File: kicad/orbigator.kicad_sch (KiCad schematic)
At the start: 0 parts

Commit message: KiCad schematic WiP
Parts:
- added BT1: CR2032, symbol Device:Battery_Cell
- added DISP1: OLED_Encoder, symbol orbigator:OLED_Encoder
- added M1: DYNAMIXEL_1, symbol Connector_Generic:Conn_01x03
- added M2: DYNAMIXEL_2, symbol Connector_Generic:Conn_01x03
- added R1, R2, R3: 10k, symbol PCM_Elektuur:R
- added RTC1: DS3232, symbol orbigator:Adafruit_DS3231_Breakout
- added U1: Pico_2, Module_RaspberryPi_Pico:RaspberryPi_Pico_Original_SMD_HandSolder, symbol MCU_Module_RaspberryPi_Pico:RaspberryPi_Pico_DebugPins
- added U2: 74LS126, symbol 74xx:74LS126
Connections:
- new net 3V3: DISP1.9 (VCC), R2.1 (+), R3.1 (+), RTC1.1 (Vin), U1.36 (3V3), U2.14 (VCC)
- new net 3V_BAT: BT1.1 (+), RTC1.5 (BAT)
- new net 5V0: M1.2 (Pin_2), M2.2 (Pin_2), R1.1 (+), U1.40 (VBUS)
- new net 5V_SYS: U1.39 (VSYS)
- new net BAK_BTN: DISP1.7 (BAK_BTN), U1.12 (GPIO9)
- new net CNF_BTN: DISP1.1 (CNF_BTN), U1.14 (GPIO10)
- new net DIR: U1.4 (GPIO2), U2.1
- new net ENC_A: DISP1.5 (ENC_A), U1.9 (GPIO6)
- new net ENC_B: DISP1.6 (ENC_B), U1.10 (GPIO7)
- new net ENC_SW: DISP1.4 (ENC_SW), U1.11 (GPIO8)
- new net GND: BT1.2 (-), DISP1.8 (GND), M1.1 (Pin_1), M2.1 (Pin_1), RTC1.2 (GND), U1.13 (GND), U1.18 (GND), U1.23 (GND), U1.28 (GND), U1.3 (GND), U1.38 (GND), U1.8 (GND), U1.D2 (GND), U2.10, U2.12, U2.13, U2.4, U2.5, U2.7 (GND), U2.9
- new net MOT_DAT: M1.3 (Pin_3), M2.3 (Pin_3), R1.2 (-), U1.2 (GPIO1), U2.3
- new net SCL: DISP1.3 (SCL), R2.2 (-), RTC1.3 (SCL), U1.7 (GPIO5)
- new net SDA: DISP1.2 (SDA), R3.2 (-), RTC1.4 (SDA), U1.6 (GPIO4)
- new net UART_TX: U1.1 (GPIO0), U2.2
- no-connect marks 0 -> 3
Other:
- company: WyoLum -> (none)
- title: Orbigator Controller -> (none)

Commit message: schematic done
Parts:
- added J1: Conn_01x01, symbol orbigator:Conn_01x01
- added J10: Conn_01x01, symbol orbigator:Conn_01x01_16
- added J11: Conn_01x01, symbol orbigator:Conn_01x01_15
- added J12: Conn_01x01, symbol orbigator:Conn_01x01_14
- added J13: Conn_01x01, symbol orbigator:Conn_01x01_13
- added J14: Conn_01x01, symbol orbigator:Conn_01x01_12
- added J15: Conn_01x01, symbol orbigator:Conn_01x01_11
- added J16: Conn_01x01, symbol orbigator:Conn_01x01_10
- added J17: Conn_01x01, symbol orbigator:Conn_01x01_9
- added J18: Conn_01x01, symbol orbigator:Conn_01x01_8
- added J19: Conn_01x01, symbol orbigator:Conn_01x01_7
- added J2: Conn_01x01, symbol orbigator:Conn_01x01_24
- added J20: Conn_01x01, symbol orbigator:Conn_01x01_6
- added J21: Conn_01x01, symbol orbigator:Conn_01x01_5
- added J22: Conn_01x01, symbol orbigator:Conn_01x01_4
- added J23: Conn_01x01, symbol orbigator:Conn_01x01_3
- added J24: Conn_01x01, symbol orbigator:Conn_01x01_2
- added J25, J26, J27, J28, J29: Conn_01x01, symbol orbigator:Conn_01x01_1
- added J3: Conn_01x01, symbol orbigator:Conn_01x01_23
- added J4: Conn_01x01, symbol orbigator:Conn_01x01_22
- added J5: Conn_01x01, symbol orbigator:Conn_01x01_21
- added J6: Conn_01x01, symbol orbigator:Conn_01x01_20
- added J7: Conn_01x01, symbol orbigator:Conn_01x01_19
- added J8: Conn_01x01, symbol orbigator:Conn_01x01_18
- added J9: Conn_01x01, symbol orbigator:Conn_01x01_17
- BT1: symbol Device:Battery_Cell -> orbigator:Battery_Cell
- M1, M2: symbol Connector_Generic:Conn_01x03 -> orbigator:Conn_01x03
- R1, R2, R3: symbol PCM_Elektuur:R -> orbigator:R
- U1: symbol MCU_Module_RaspberryPi_Pico:RaspberryPi_Pico_DebugPins -> orbigator:RaspberryPi_Pico_DebugPins
- U2: symbol 74xx:74LS126 -> orbigator:74LS126
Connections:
- net 3V3: now also R1.1 (+), J23.1 (Pin_1)
- net 5V0: now also J25.1 (Pin_1); no longer R1.1 (+)
- net 5V_SYS: now also J24.1 (Pin_1)
- net GND: now also J26.1 (Pin_1)
- net at U1.15 (GPIO11): now also J19.1 (Pin_1)
- net at U1.16 (GPIO12): now also J18.1 (Pin_1)
- net at U1.17 (GPIO13): now also J17.1 (Pin_1)
- net at U1.19 (GPIO14): now also J16.1 (Pin_1)
- net at U1.20 (GPIO15): now also J15.1 (Pin_1)
- net at U1.21 (GPIO16): now also J1.1 (Pin_1)
- net at U1.22 (GPIO17): now also J2.1 (Pin_1)
- net at U1.24 (GPIO18): now also J3.1 (Pin_1)
- net at U1.25 (GPIO19): now also J4.1 (Pin_1)
- net at U1.26 (GPIO20): now also J5.1 (Pin_1)
- net at U1.27 (GPIO21): now also J6.1 (Pin_1)
- net at U1.29 (GPIO22): now also J7.1 (Pin_1)
- net at U1.30 (RUN): now also J14.1 (Pin_1)
- net at U1.31 (GPIO26_ADC0): now also J9.1 (Pin_1)
- net at U1.32 (GPIO27_ADC1): now also J10.1 (Pin_1)
- net at U1.33 (AGND): now also J12.1 (Pin_1)
- net at U1.34 (GPIO28_ADC2): now also J11.1 (Pin_1)
- net at U1.35 (ADC_VREF): now also J8.1 (Pin_1)
- net at U1.37 (3V3_EN): now also J13.1 (Pin_1)
- net at U1.5 (GPIO3): now also J20.1 (Pin_1)
- net at U1.D1 (SWCLK): now also J22.1 (Pin_1)
- net at U1.D3 (SWDIO): now also J21.1 (Pin_1)
- net at RTC1.6 (32k): now also J27.1 (Pin_1)
- net at RTC1.7 (SQW): now also J28.1 (Pin_1)
- net at RTC1.8 (RST): now also J29.1 (Pin_1)
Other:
- company: (none) -> Wyolum
- title: (none) -> Orbigator PCB

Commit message: PCB layout WiP
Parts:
- removed BT1: CR2032, symbol orbigator:Battery_Cell
- removed J27, J28, J29: Conn_01x01, symbol orbigator:Conn_01x01_1
- removed RTC1: DS3232, symbol orbigator:Adafruit_DS3231_Breakout
- added H1, H2, H3, H4: MountingHole, orbigator:MountingHole_3.2mm_M3, symbol Mechanical:MountingHole
- added RTC1: DS3232, orbigator:DS3232_RTC, symbol Connector_Generic:Conn_01x07
- DISP1: footprint (none) -> orbigator:PinSocket_1x09_P2.54mm_Vertical
- J1, J10, J11, J12, J13, J14, J15, J16, J17, J18, J19, J2, J20, J21, J22, J23, J24, J25, J26, J3, J4, J5, J6, J7, J8, J9: footprint (none) -> orbigator:PinHeader_1x01_P2.54mm_Vertical
- M1, M2: footprint (none) -> orbigator:JST_GH_BM03B-GHS-TBT_1x03-1MP_P1.25mm_Vertical
- R1, R2, R3: footprint (none) -> orbigator:R_Axial_DIN0207_L6.3mm_D2.5mm_P7.62mm_Horizontal
- U1: footprint Module_RaspberryPi_Pico:RaspberryPi_Pico_Original_SMD_HandSolder -> orbigator:RaspberryPi_Pico_SMD_HandSolder
- U2: footprint (none) -> orbigator:DIP-14_W7.62mm
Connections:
- net 3V3: now also RTC1.1 (Pin_1)
- net GND: now also RTC1.2 (Pin_2)
- net SCL: now also RTC1.3 (Pin_3)
- net SDA: now also RTC1.4 (Pin_4)
- new net 32k: RTC1.7 (Pin_7)
- new net INT: RTC1.5 (Pin_5)
- new net RST: RTC1.6 (Pin_6)
- no-connect marks 3 -> 6

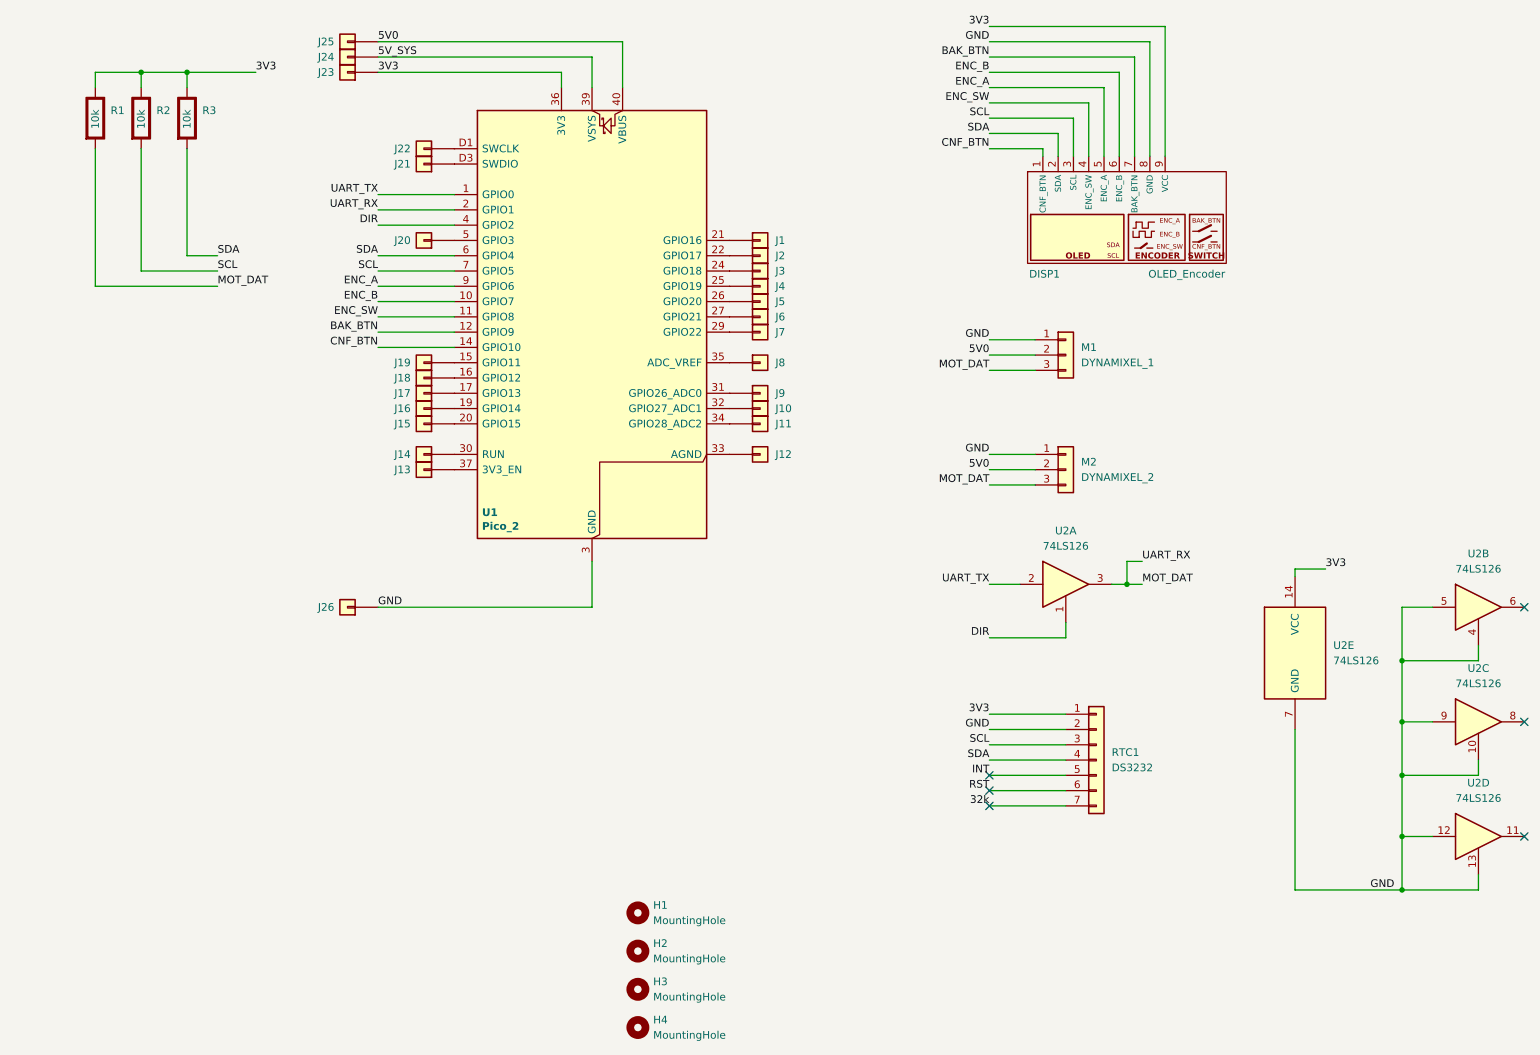
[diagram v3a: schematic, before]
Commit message: PCB check parts placement
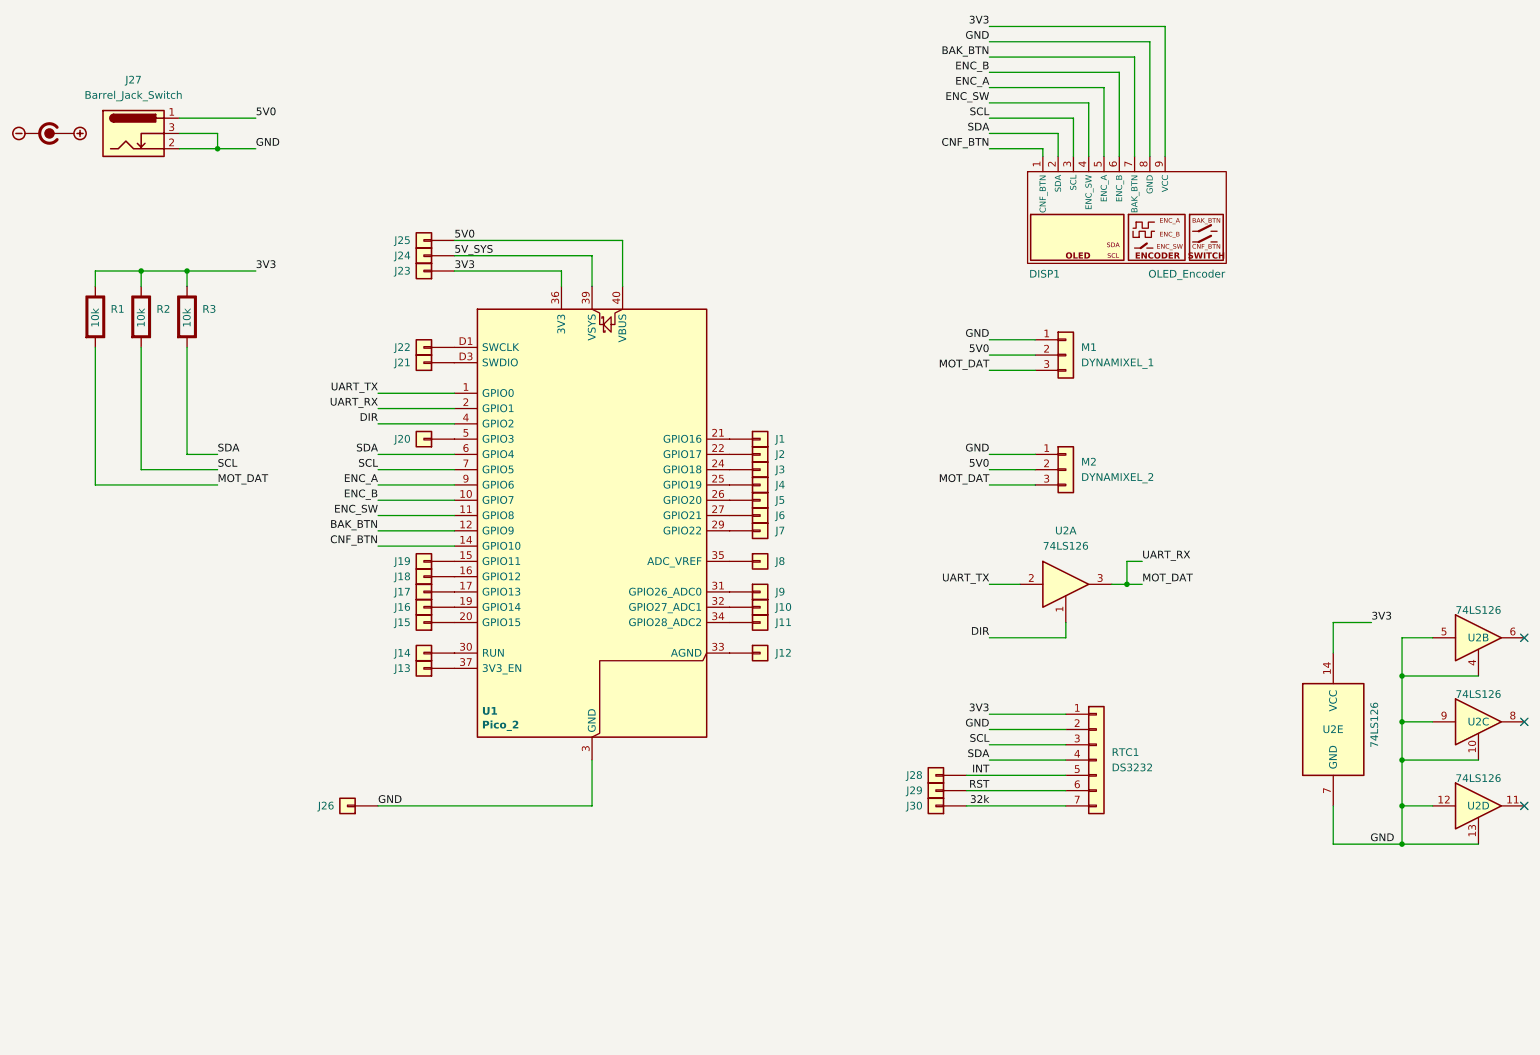
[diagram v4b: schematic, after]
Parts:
- removed H1, H2, H3, H4: MountingHole, orbigator:MountingHole_3.2mm_M3, symbol Mechanical:MountingHole
- added J27: Barrel_Jack_Switch, orbigator:BarrelJack_Horizontal, symbol Connector:Barrel_Jack_Switch
- added J28, J29, J30: Conn_01x01, orbigator:PinHeader_1x01_P2.54mm_Vertical, symbol orbigator:Conn_01x01_1
- added U3: DC_polarity, orbigator:DC, symbol orbigator:DC
- DISP1: footprint orbigator:PinSocket_1x09_P2.54mm_Vertical -> orbigator:OLED_ENC2
- M1, M2: footprint orbigator:JST_GH_BM03B-GHS-TBT_1x03-1MP_P1.25mm_Vertical -> orbigator:JST_EH_B3B-EH-A_1x03_P2.50mm_Vertical
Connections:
- net 32k: now also J30.1 (Pin_1)
- net 5V0: now also J27.1
- net GND: now also J27.2, J27.3
- net INT: now also J28.1 (Pin_1)
- net RST: now also J29.1 (Pin_1)
- no-connect marks 6 -> 3
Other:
- moved on the sheet: J1, J10, J11, J12, J13, J14, J15, J16, J17, J18, J19, J2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

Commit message: PCB layout done
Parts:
- added J31, J32, J33, J34, J35, J36, J37: Conn_01x01, orbigator:PinHeader_1x01_P2.54mm_Vertical, symbol orbigator:Conn_01x01_1
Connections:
- net GND: now also J12.1 (Pin_1), U1.33 (AGND), J31.1 (Pin_1), J32.1 (Pin_1), J33.1 (Pin_1), J34.1 (Pin_1), J35.1 (Pin_1), J36.1 (Pin_1), J37.1 (Pin_1)
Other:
- moved on the sheet: J12

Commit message: PCB layout please verify
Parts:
- DISP1: footprint orbigator:OLED_ENC2 -> orbigator:OLED_ENC3
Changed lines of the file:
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@@
 			)
 		)
-		(property "Footprint" "orbigator:OLED_ENC2"
+		(property "Footprint" "orbigator:OLED_ENC3"
 			(at 194.31 41.91 0)
 			(effects

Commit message: gerbers
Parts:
- RTC1: footprint orbigator:DS3232_RTC -> orbigator:DS3232_RTC_vert
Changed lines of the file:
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@@
 			)
 		)
-		(property "Footprint" "orbigator:DS3232_RTC"
+		(property "Footprint" "orbigator:DS3232_RTC_vert"
 			(at 203.2 139.7 0)
 			(effects
